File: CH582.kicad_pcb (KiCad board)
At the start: 2 copper layers, 32 x 32 mm, 48 parts, among them J1 Conn_01x02, J3 USB, J4 Conn_02x04_Odd_Even, J5 Pogo Pin Socket 2.54, Q1 NPN, N.C., U2 TP4056, U4 M3406, Y1 32MHz, Y2 Crystal_Small

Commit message: GROUND VIASgit add -A
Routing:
- net GND: track 76.1 -> 70.4 mm, vias 32 -> 41
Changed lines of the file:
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@@
     )
     (stroke (width 0) (type solid)) (fill solid) (layer "F.Cu"))
-  (gr_line (start 24.9385 23.1355) (end 26.289 24.384)
-    (stroke (width 0.2) (type solid)) (layer "F.Cu"))
   (gr_rect (start 35.9242 36.6498) (end 46.9242 46.8878)
     (stroke (width 0.2) (type solid)) (fill none) (layer "F.SilkS"))
@@
   (segment (start 19.880472 40.767) (end 20.4415 40.767) (width 0.5) (layer "F.Cu") (net 1))
   (segment (start 36.957 27.559) (end 36.957 27.94) (width 0.5) (layer "F.Cu") (net 1))
+  (segment (start 25.147 23.157) (end 26.247 24.257) (width 0.32) (layer "F.Cu") (net 1))
   (segment (start 44 40.2495) (end 44.0495 40.2) (width 0.5) (layer "F.Cu") (net 1))
-  (segment (start 24.937 23.157) (end 25.045 23.157) (width 0.1) (layer "F.Cu") (net 1))
+  (segment (start 24.937 23.157) (end 25.147 23.157) (width 0.32) (layer "F.Cu") (net 1))
   (segment (start 28.698 44.2) (end 30 44.2) (width 0.5) (layer "F.Cu") (net 1))
   (segment (start 30.097 38.481) (end 29.083 38.481) (width 0.5) (layer "F.Cu") (net 1))
@@
   (segment (start 37.721 28.704) (end 37.721 31.5) (width 0.5) (layer "F.Cu") (net 1))
   (segment (start 24.275 39.985) (end 24.275 39.8) (width 0.5) (layer "F.Cu") (net 1))
-  (segment (start 25.045 23.157) (end 26.145 24.257) (width 0.1) (layer "F.Cu") (net 1))
   (segment (start 34.8 37.4) (end 35.15 37.05) (width 0.5) (layer "F.Cu") (net 1))
   (segment (start 24.524 21.831) (end 23.114 21.831) (width 0.5) (layer "F.Cu") (net 1))
@@
   (segment (start 39.9992 41.2878) (end 41.0338 41.2878) (width 0.32) (layer "F.Cu") (net 1))
   (segment (start 41.529 42.5503) (end 41.7617 42.5503) (width 0.32) (layer "F.Cu") (net 1))
-  (segment (start 26.145 24.257) (end 26.337 24.257) (width 0.1) (layer "F.Cu") (net 1))
+  (segment (start 26.337 24.257) (end 27.178 24.257) (width 0.32) (layer "F.Cu") (net 1))
   (segment (start 22.72 42.98) (end 22.72 41.755) (width 0.5) (layer "F.Cu") (net 1))
   (segment (start 41.7645 43.7765) (end 42.9765 43.7765) (width 0.5) (layer "F.Cu") (net 1))
+  (segment (start 26.247 24.257) (end 26.337 24.257) (width 0.32) (layer "F.Cu") (net 1))
   (segment (start 22.225 33.0505) (end 21.8135 32.639) (width 0.5) (layer "F.Cu") (net 1))
   (segment (start 36.957 27.94) (end 37.721 28.704) (width 0.5) (layer "F.Cu") (net 1))
   (segment (start 15.875 43) (end 17 44.125) (width 0.5) (layer "F.Cu") (net 1))
-  (segment (start 27.686 24.003) (end 27.432 24.257) (width 0.5) (layer "F.Cu") (net 1))
   (segment (start 30.7132 40.7878) (end 30.734 40.767) (width 0.5) (layer "F.Cu") (net 1))
   (segment (start 22.99 43.25) (end 22.72 42.98) (width 0.5) (layer "F.Cu") (net 1))
@@
   (segment (start 18.034 38.173472) (end 19.279 39.418472) (width 0.5) (layer "F.Cu") (net 1))
   (segment (start 25.273 21.082) (end 24.524 21.831) (width 0.5) (layer "F.Cu") (net 1))
-  (segment (start 27.432 24.257) (end 26.337 24.257) (width 0.5) (layer "F.Cu") (net 1))
   (segment (start 17.8492 36.6452) (end 16.891 35.687) (width 0.5) (layer "F.Cu") (net 1))
   (segment (start 36.957 27.559) (end 37.465 27.051) (width 0.5) (layer "F.Cu") (net 1))
@@
   (segment (start 16.764 35.56) (end 16.891 35.687) (width 0.32) (layer "F.Cu") (net 1))
   (via (at 27.698 45.2) (size 0.8) (drill 0.4) (layers "F.Cu" "B.Cu") (net 1))
-  (via (at 33.02 24.003) (size 0.8) (drill 0.4) (layers "F.Cu" "B.Cu") (net 1))
+  (via (at 34.29 23.749) (size 0.8) (drill 0.4) (layers "F.Cu" "B.Cu") (net 1))
   (via (at 46.101 38.481) (size 0.8) (drill 0.4) (layers "F.Cu" "B.Cu") (net 1))
+  (via (at 15.7734 24.0538) (size 0.8) (drill 0.4) (layers "F.Cu" "B.Cu") (free) (net 1))
   (via (at 20.955 46.355) (size 0.8) (drill 0.4) (layers "F.Cu" "B.Cu") (free) (net 1))
   (via (at 41.275 41.529) (size 0.8) (drill 0.4) (layers "F.Cu" "B.Cu") (net 1))
@@
   (via (at 29.083 38.481) (size 0.8) (drill 0.4) (layers "F.Cu" "B.Cu") (net 1))
   (via (at 15.494 46.355) (size 0.8) (drill 0.4) (layers "F.Cu" "B.Cu") (free) (net 1))
+  (via (at 33.274 26.797) (size 0.8) (drill 0.4) (layers "F.Cu" "B.Cu") (free) (net 1))
+  (via (at 18.669 24.0792) (size 0.8) (drill 0.4) (layers "F.Cu" "B.Cu") (free) (net 1))
   (via (at 39.37 44.831) (size 0.8) (drill 0.4) (layers "F.Cu" "B.Cu") (net 1))
   (via (at 25.273 21.082) (size 0.8) (drill 0.4) (layers "F.Cu" "B.Cu") (net 1))
@@
   (via (at 27.59075 36.41725) (size 0.8) (drill 0.4) (layers "F.Cu" "B.Cu") (net 1))
   (via (at 30.734 40.767) (size 0.8) (drill 0.4) (layers "F.Cu" "B.Cu") (net 1))
+  (via (at 41.1734 35.5092) (size 0.8) (drill 0.4) (layers "F.Cu" "B.Cu") (free) (net 1))
   (via (at 34.8 37.4) (size 0.8) (drill 0.4) (layers "F.Cu" "B.Cu") (net 1))
+  (via (at 37.465 44.323) (size 0.8) (drill 0.4) (layers "F.Cu" "B.Cu") (free) (net 1))
   (via (at 18.034 38.1) (size 0.8) (drill 0.4) (layers "F.Cu" "B.Cu") (net 1))
   (via (at 20.955 36.449) (size 0.8) (drill 0.4) (layers "F.Cu" "B.Cu") (free) (net 1))
-  (via (at 16.002 21.082) (size 0.8) (drill 0.4) (layers "F.Cu" "B.Cu") (net 1))
-  (via (at 27.686 24.003) (size 0.8) (drill 0.4) (layers "F.Cu" "B.Cu") (free) (net 1))
+  (via (at 15.748 21.082) (size 0.8) (drill 0.4) (layers "F.Cu" "B.Cu") (net 1))
+  (via (at 29.718 23.749) (size 0.8) (drill 0.4) (layers "F.Cu" "B.Cu") (free) (net 1))
   (via (at 44.0495 40.2) (size 0.8) (drill 0.4) (layers "F.Cu" "B.Cu") (net 1))
   (via (at 32.893 40.767) (size 0.8) (drill 0.4) (layers "F.Cu" "B.Cu") (free) (net 1))
   (via (at 24.683071 40.696081) (size 0.8) (drill 0.4) (layers "F.Cu" "B.Cu") (net 1))
-  (via (at 34.798 43.688) (size 0.8) (drill 0.4) (layers "F.Cu" "B.Cu") (net 1))
+  (via (at 44.069 25.4) (size 0.8) (drill 0.4) (layers "F.Cu" "B.Cu") (free) (net 1))
+  (via (at 35.433 43.307) (size 0.8) (drill 0.4) (layers "F.Cu" "B.Cu") (net 1))
+  (via (at 46.101 35.179) (size 0.8) (drill 0.4) (layers "F.Cu" "B.Cu") (free) (net 1))
+  (via (at 28.0162 32.9692) (size 0.8) (drill 0.4) (layers "F.Cu" "B.Cu") (free) (net 1))
   (via (at 46.101 42.418) (size 0.8) (drill 0.4) (layers "F.Cu" "B.Cu") (net 1))
   (via (at 41.275 46.101) (size 0.8) (drill 0.4) (layers "F.Cu" "B.Cu") (net 1))
@@
   (via (at 29.718 21.082) (size 0.8) (drill 0.4) (layers "F.Cu" "B.Cu") (free) (net 1))
   (via (at 34.29 21.082) (size 0.8) (drill 0.4) (layers "F.Cu" "B.Cu") (free) (net 1))
+  (via (at 28.702 34.544) (size 0.8) (drill 0.4) (layers "F.Cu" "B.Cu") (free) (net 1))
   (via (at 15.875 43) (size 0.8) (drill 0.4) (layers "F.Cu" "B.Cu") (net 1))
   (via (at 43 43.8) (size 0.8) (drill 0.4) (layers "F.Cu" "B.Cu") (net 1))
   (via (at 23.749 37.719) (size 0.8) (drill 0.4) (layers "F.Cu" "B.Cu") (free) (net 1))
   (segment (start 30.669 45.655) (end 34.267918 45.655) (width 0.5) (layer "B.Cu") (net 1))
-  (segment (start 38.862 44.323) (end 39.37 44.831) (width 0.5) (layer "B.Cu") (net 1))
   (segment (start 30 44.2) (end 30 44.986) (width 0.5) (layer "B.Cu") (net 1))
   (segment (start 22.225 33.0505) (end 24.224 33.0505) (width 0.5) (layer "B.Cu") (net 1))
+  (segment (start 34.355 45.655) (end 34.798 45.212) (width 0.5) (layer "B.Cu") (net 1))
   (segment (start 29.083 37.9095) (end 29.083 38.481) (width 0.5) (layer "B.Cu") (net 1))
   (segment (start 24.224 33.0505) (end 27.59075 36.41725) (width 0.5) (layer "B.Cu") (net 1))
+  (segment (start 34.267918 45.655) (end 34.355 45.655) (width 0.5) (layer "B.Cu") (net 1))
   (segment (start 30 44.986) (end 30.669 45.655) (width 0.5) (layer "B.Cu") (net 1))
-  (segment (start 35.599918 44.323) (end 38.862 44.323) (width 0.5) (layer "B.Cu") (net 1))
   (segment (start 27.59075 36.41725) (end 29.083 37.9095) (width 0.5) (layer "B.Cu") (net 1))
-  (segment (start 34.267918 45.655) (end 35.599918 44.323) (width 0.5) (layer "B.Cu") (net 1))
   (segment (start 20.25 23.639376) (end 20.210376 23.639376) (width 0.5) (layer "F.Cu") (net 2))
   (segment (start 20.210376 23.639376) (end 16.5 19.929) (width 0.5) (layer "F.Cu") (net 2))

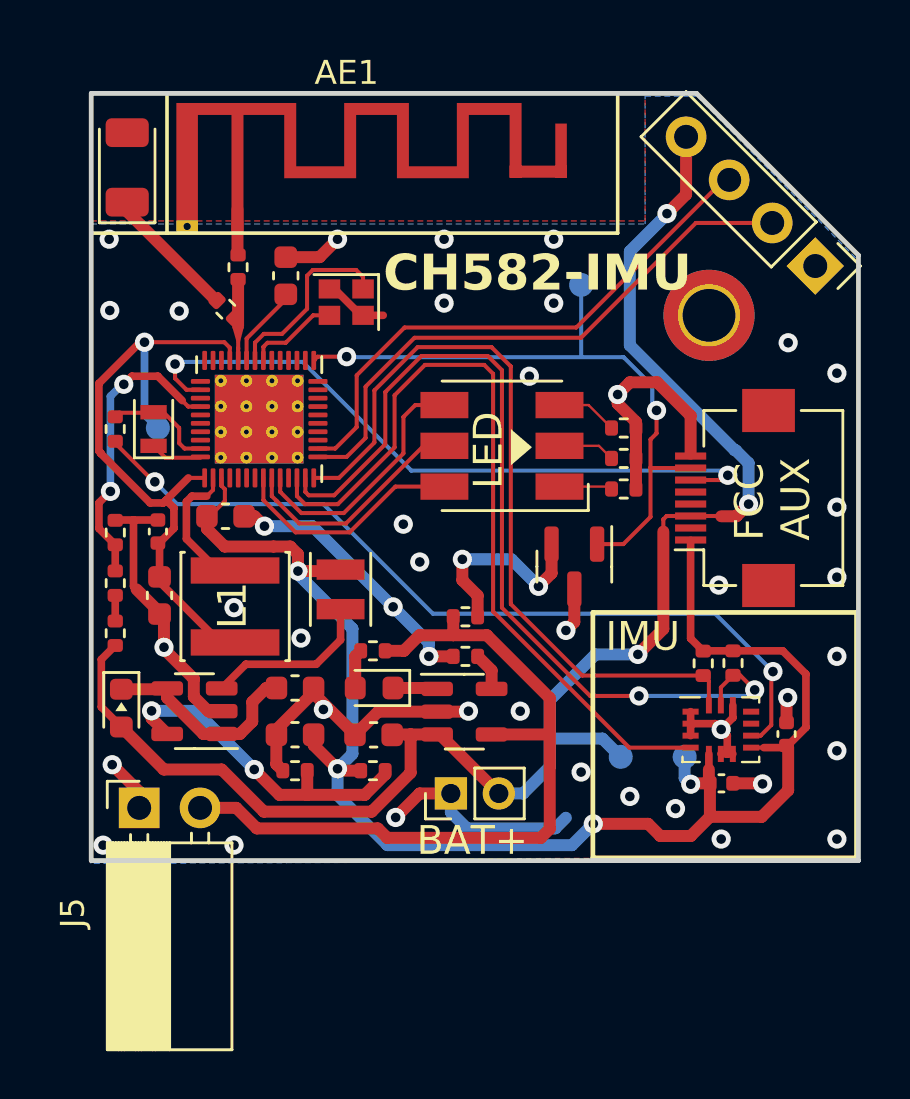
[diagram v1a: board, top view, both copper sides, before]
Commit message: fixed clearance issues
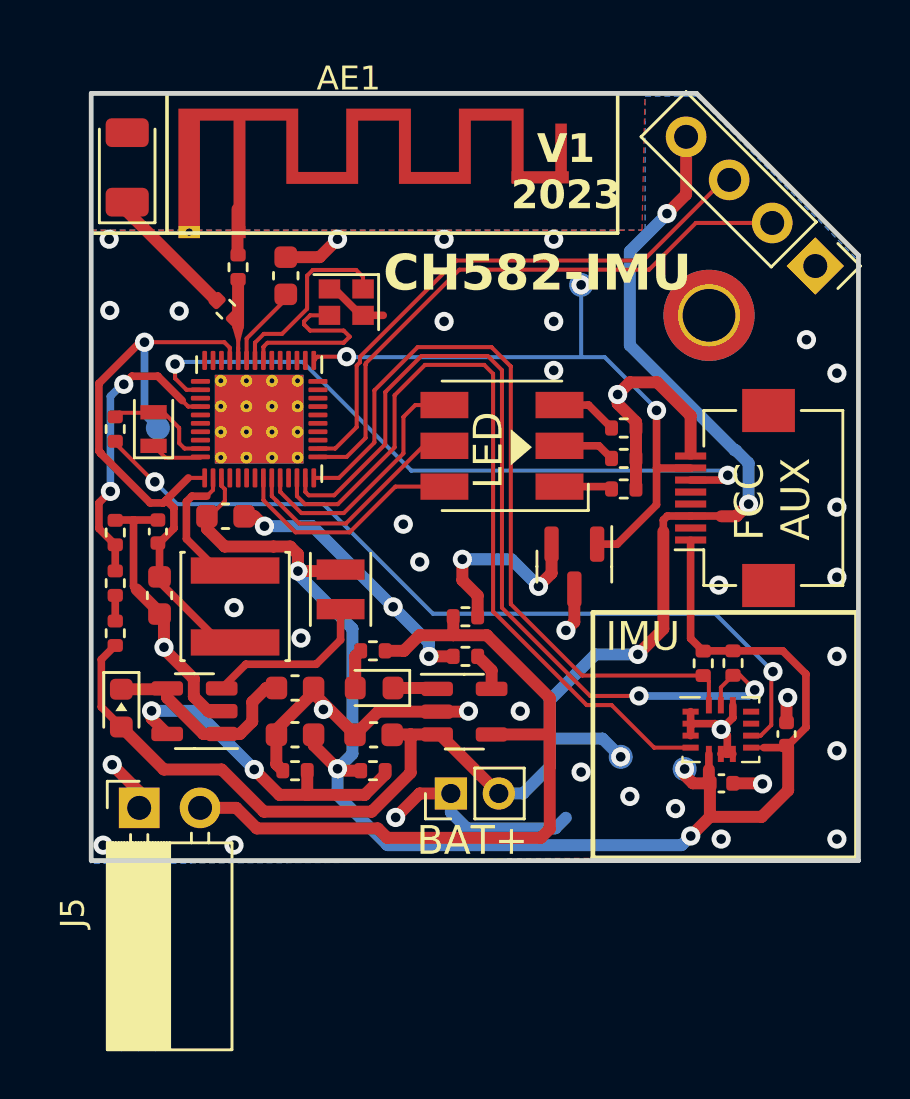
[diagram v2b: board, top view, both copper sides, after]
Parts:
- moved 3V1 0.51 mm to (39.8, 43.2)
- moved AE1 0.25 mm to (21.2, 20.8)
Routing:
- net X32MO: track 3.87 -> 7.75 mm
- net +3V3: track 64.6 -> 63.5 mm
- net G_RST: track 27.7 -> 26.8 mm, vias 2 -> 3
- net USB_D+: track 24.2 -> 24.8 mm
- net /B+: vias 3 -> 4
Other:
- board text removed: "L1"

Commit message: final tweaks 1
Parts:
- added R17: 200k, Resistor_SMD:R_0402_1005Metric, F.Cu at (44.8, 39.4)
- D2: value Zener -> Schottky
- moved R13 0.64 mm to (37.2, 30.9)
- moved R8 0.38 mm to (37.2, 29.8)
- moved R1 0.13 mm to (30.5, 36.8)
- moved R4 0.13 mm to (30.5, 38.5)
- moved R6 0.13 mm to (37.2, 28.8)
- moved AE1 0.10 mm to (21.1, 20.8)
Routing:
- net GND: track 70.4 -> 73.0 mm, vias 41 -> 42
- net ICM_CLK: track 34.7 -> 35.7 mm
- net Net-(Q1-B): track 8.29 -> 7.34 mm

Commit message: V1, order version
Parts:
- added C10: 10nF, Capacitor_SMD:C_0402_1005Metric, F.Cu at (16.4, 25.7)
- added TCK1: SWD_TCK, TestPoint:TestPoint_Pad_D1.0mm, B.Cu at (32.1, 27.9)
- R3: renamed from R17; value 200k -> N.C.
- moved 3V1 1.48 mm to (39.0, 44.5)
- moved C8 0.20 mm to (17.7, 35.9)
- moved L1 0.17 mm to (20.8, 36.4)
- moved C2 0.13 mm to (17.7, 33.3)
- renumbered R9 to R10, R10 to R11, R11 to R12, R12 to R13, R13 to R14, R14 to R15, R15 to R16, R16 to R17, R3 to R4, R4 to R5, R5 to R6, R6 to R7, R7 to R8, R8 to R9
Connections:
- U3 pad 11: unconnected-(U3-MISO_/DTR-Pad11) -> TCK
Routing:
- net TCK: track 0.00 -> 13.9 mm, vias 0 -> 1
- net VDCIA: track 27.7 -> 34.5 mm
- net +3V3: track 64.0 -> 66.7 mm
- net GND: track 73.0 -> 74.8 mm, vias 42 -> 41
- net SCL: track 37.6 -> 38.8 mm
- net Net-(D3-BA): track 10.6 -> 11.4 mm
- net ICM_CLK: track 35.7 -> 36.6 mm
- net ADC: track 12.4 -> 13.2 mm
- net Net-(D3-RA): track 9.83 -> 10.4 mm
- net Net-(D3-GA): track 9.77 -> 10.3 mm
